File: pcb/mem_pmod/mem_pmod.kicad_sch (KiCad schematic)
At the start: 12 parts, among them J1 Conn_01x04_Pin, U1 74HC125D

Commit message: more or less completed schematic. Still needs caps/resistors or whatever
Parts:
- removed U1: 74HC125D, SOIC14_TOS, symbol 74HC125D:74HC125D
- removed VRAM1: APS6404L-3SQR-SN, APS6404L-3SQR-SN_APY, symbol ul_APS6404L-3SQR-SN:APS6404L-3SQR-SN
- added A0_NAND1, A0_NAND2, A1_NAND1: NC7SZ86FHX, MICROPAK2-6_1X1_ONS, symbol 74LVC1G57FW4-7:NC7SZ86FHX
- added J2: Conn_01x02_Pin, Connector_PinHeader_2.54mm:PinHeader_1x02_P2.54mm_Horizontal, symbol Connector:Conn_01x02_Pin
- added PMOD2: PMOD-Device-x2-Type-1A-GPIO, pmod-conn_6x2:pmod_pin_array_6x2, symbol pmod:PMOD-Device-x2-Type-1A-GPIO
- added U2: NL17SV32XV5T2G, SOT553-5_ONS, symbol NL17SV32XV5T2G:NL17SV32XV5T2G
- added XOR1: NC7SZ86FHX, MICROPAK2-6_1X1_ONS, symbol NC7SZ86FHX:NC7SZ86FHX
- J1: footprint (none) -> Connector_PinHeader_2.54mm:PinHeader_1x04_P2.54mm_Horizontal
- renumbered Clock_Divider to Clock_Divider1, Flash to Flash1, RAM0 to RAM1, RAM1 to RAM2, RAM2 to RAM3, VGA_DFLIP to VGA_DFLIP1, VGA_DFLIP to VGA_DFLIP2, VRAM0 to VRAM1
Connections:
- net RAM_VS0 is gone; now on net CS_V0: VRAM1.1 (/CE)
- net CS_A0: now also A0_NAND1.1 (A), A0_NAND2.1 (A), U2.1 (B), XOR1.1 (A)
- net CS_A1: now also A0_NAND2.2 (B), A1_NAND1.1 (A), U2.2 (A), XOR1.2 (B)
- net GND: now also A0_NAND1.3 (GND), A0_NAND2.3 (GND), A1_NAND1.3 (GND), PMOD2.11 (GND), PMOD2.5 (GND), U2.3 (GND), XOR1.3 (GND)
- net PMOD_B0: now also VGA_DFLIP1.3 (1D), VGA_DFLIP2.3 (1D)
- net PMOD_B1: now also VGA_DFLIP1.4 (2D), VGA_DFLIP2.4 (2D)
- net PMOD_B2: now also VGA_DFLIP1.7 (3D), VGA_DFLIP2.7 (3D)
- net RAM_CS0: now also A0_NAND1.4 (Y)
- net RAM_CS1: now also A1_NAND1.4 (Y)
- net RAM_CS2: now also U2.4 (Y)
- net RAM_CS3: now also A0_NAND2.4 (Y)
- net VCC: now also A0_NAND1.6 (VCC), A0_NAND2.6 (VCC), A1_NAND1.6 (VCC), PMOD2.12 (VCC), PMOD2.6 (VCC), U2.6 (VCC), XOR1.6 (VCC)
- net FLIP_2: now reaches VGA_DFLIP1.14 (6D)
- net FLIP_2: now also VGA_DFLIP1.6 (3Q)
- net VGA_B_1: now reaches VGA_DFLIP1.15 (6Q)
- net VGA_B_1: now also PMOD2.3 (IOA2)
- net VGA_G_1: now reaches VGA_DFLIP1.16 (7Q)
- net VGA_G_1: now also PMOD2.2 (IOA1)
- net FLIP_1: now reaches VGA_DFLIP1.17 (7D)
- net FLIP_1: now also VGA_DFLIP1.5 (2Q)
- net FLIP_0: now reaches VGA_DFLIP1.18 (8D)
- net FLIP_0: now also VGA_DFLIP1.2 (1Q)
- net VGA_R_1: now reaches VGA_DFLIP1.19 (8Q)
- net VGA_R_1: now also PMOD2.1 (IOA0)
- net VGA_R_0: now reaches VGA_DFLIP2.2 (1Q)
- net VGA_R_0: now also PMOD2.7 (IOB0)
- net VGA_G_0: now reaches VGA_DFLIP2.5 (2Q)
- net VGA_G_0: now also PMOD2.8 (IOB1)
- net VGA_B_0: now reaches VGA_DFLIP2.6 (3Q)
- net VGA_B_0: now also PMOD2.9 (IOB2)
- new net HSYNC: J2.2 (Pin_2), PMOD2.10 (IOB3)
- new net VSYNC: J2.1 (Pin_1), PMOD2.4 (IOA3)
- new net XOR_Result: A0_NAND1.2 (B), A1_NAND1.2 (B), XOR1.4 (Y)
- no-connect marks 0 -> 17
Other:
- moved on the sheet: VGA_DFLIP1, VGA_DFLIP2

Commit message: Add tinyvga and remove autosaves
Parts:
- removed PMOD2: PMOD-Device-x2-Type-1A-GPIO, pmod-conn_6x2:pmod_pin_array_6x2, symbol pmod:PMOD-Device-x2-Type-1A-GPIO
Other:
- added sheet vga (vga_submodule.kicad_sch)

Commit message: Abstracted CS stuff away into another sheet
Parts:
- removed A0_NAND1, A0_NAND2, A1_NAND1: NC7SZ86FHX, MICROPAK2-6_1X1_ONS, symbol 74LVC1G57FW4-7:NC7SZ86FHX
- removed U2: NL17SV32XV5T2G, SOT553-5_ONS, symbol NL17SV32XV5T2G:NL17SV32XV5T2G
- removed XOR1: NC7SZ86FHX, MICROPAK2-6_1X1_ONS, symbol NC7SZ86FHX:NC7SZ86FHX
- added C1: 10nF, Capacitor_SMD:C_01005_0402Metric, symbol Device:C
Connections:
- net FLIP_0: now also VGA_DFLIP2.18 (8D); no longer VGA_DFLIP1.18 (8D)
- net FLIP_1: now also VGA_DFLIP2.17 (7D); no longer VGA_DFLIP1.17 (7D)
- net FLIP_2: now also VGA_DFLIP2.14 (6D); no longer VGA_DFLIP1.14 (6D)
- net PRJ_Clock: now also Clock_Divider1.3 (*CLK); no longer Clock_Divider1.2 (CLK)
- net VCC: now also C1.1
- net VGA_B_1: now also VGA_DFLIP2.15 (6Q); no longer VGA_DFLIP1.15 (6Q)
- net VGA_G_1: now also VGA_DFLIP2.16 (7Q); no longer VGA_DFLIP1.16 (7Q)
- net VGA_R_1: now also VGA_DFLIP2.19 (8Q); no longer VGA_DFLIP1.19 (8Q)
- net VBB_CLK: now reaches Clock_Divider1.4 (VBB)
- net VBB_CLK: now also Clock_Divider1.2 (CLK)
- no-connect marks 17 -> 13
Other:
- added sheet CS_Circuit (cs_circuit.kicad_sch)

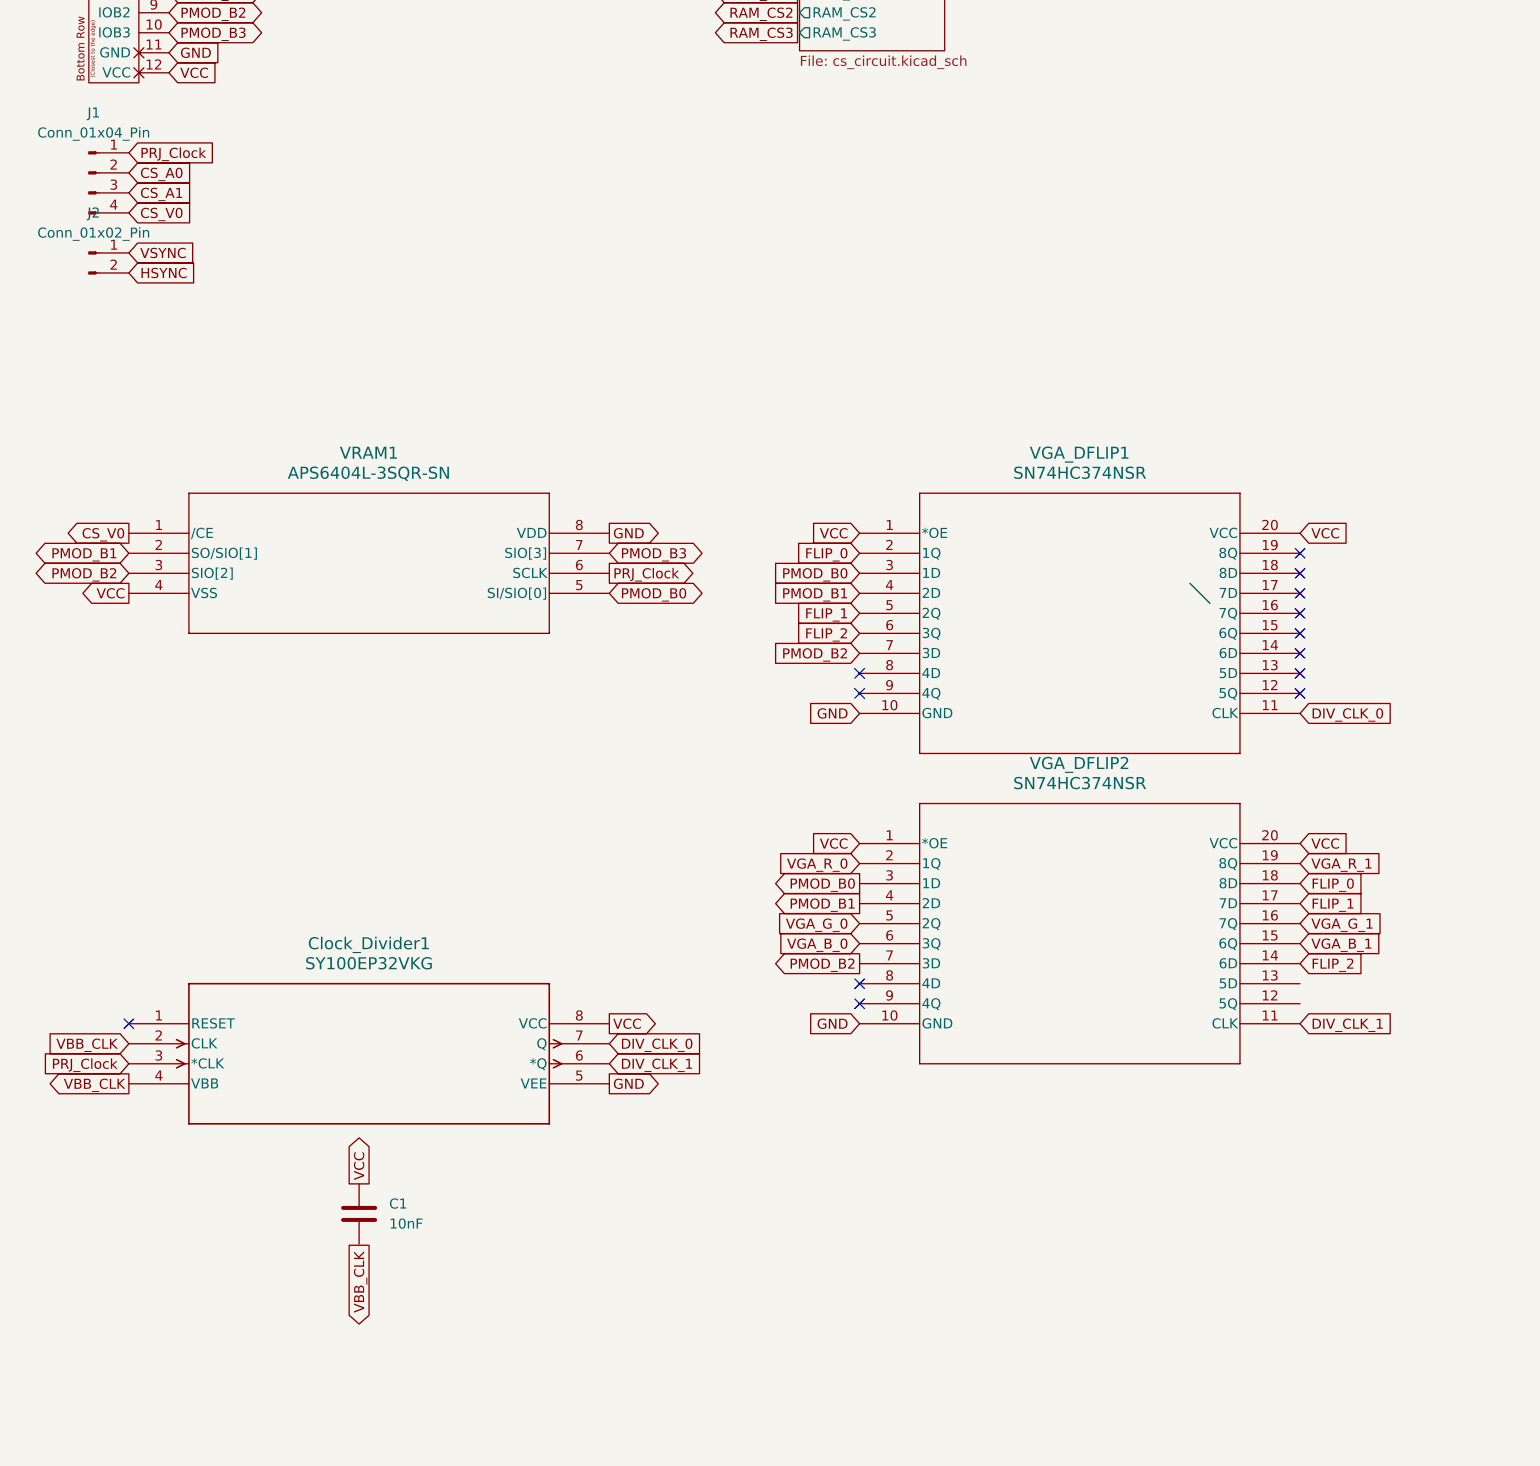
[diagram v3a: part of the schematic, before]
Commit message: change vram wiring
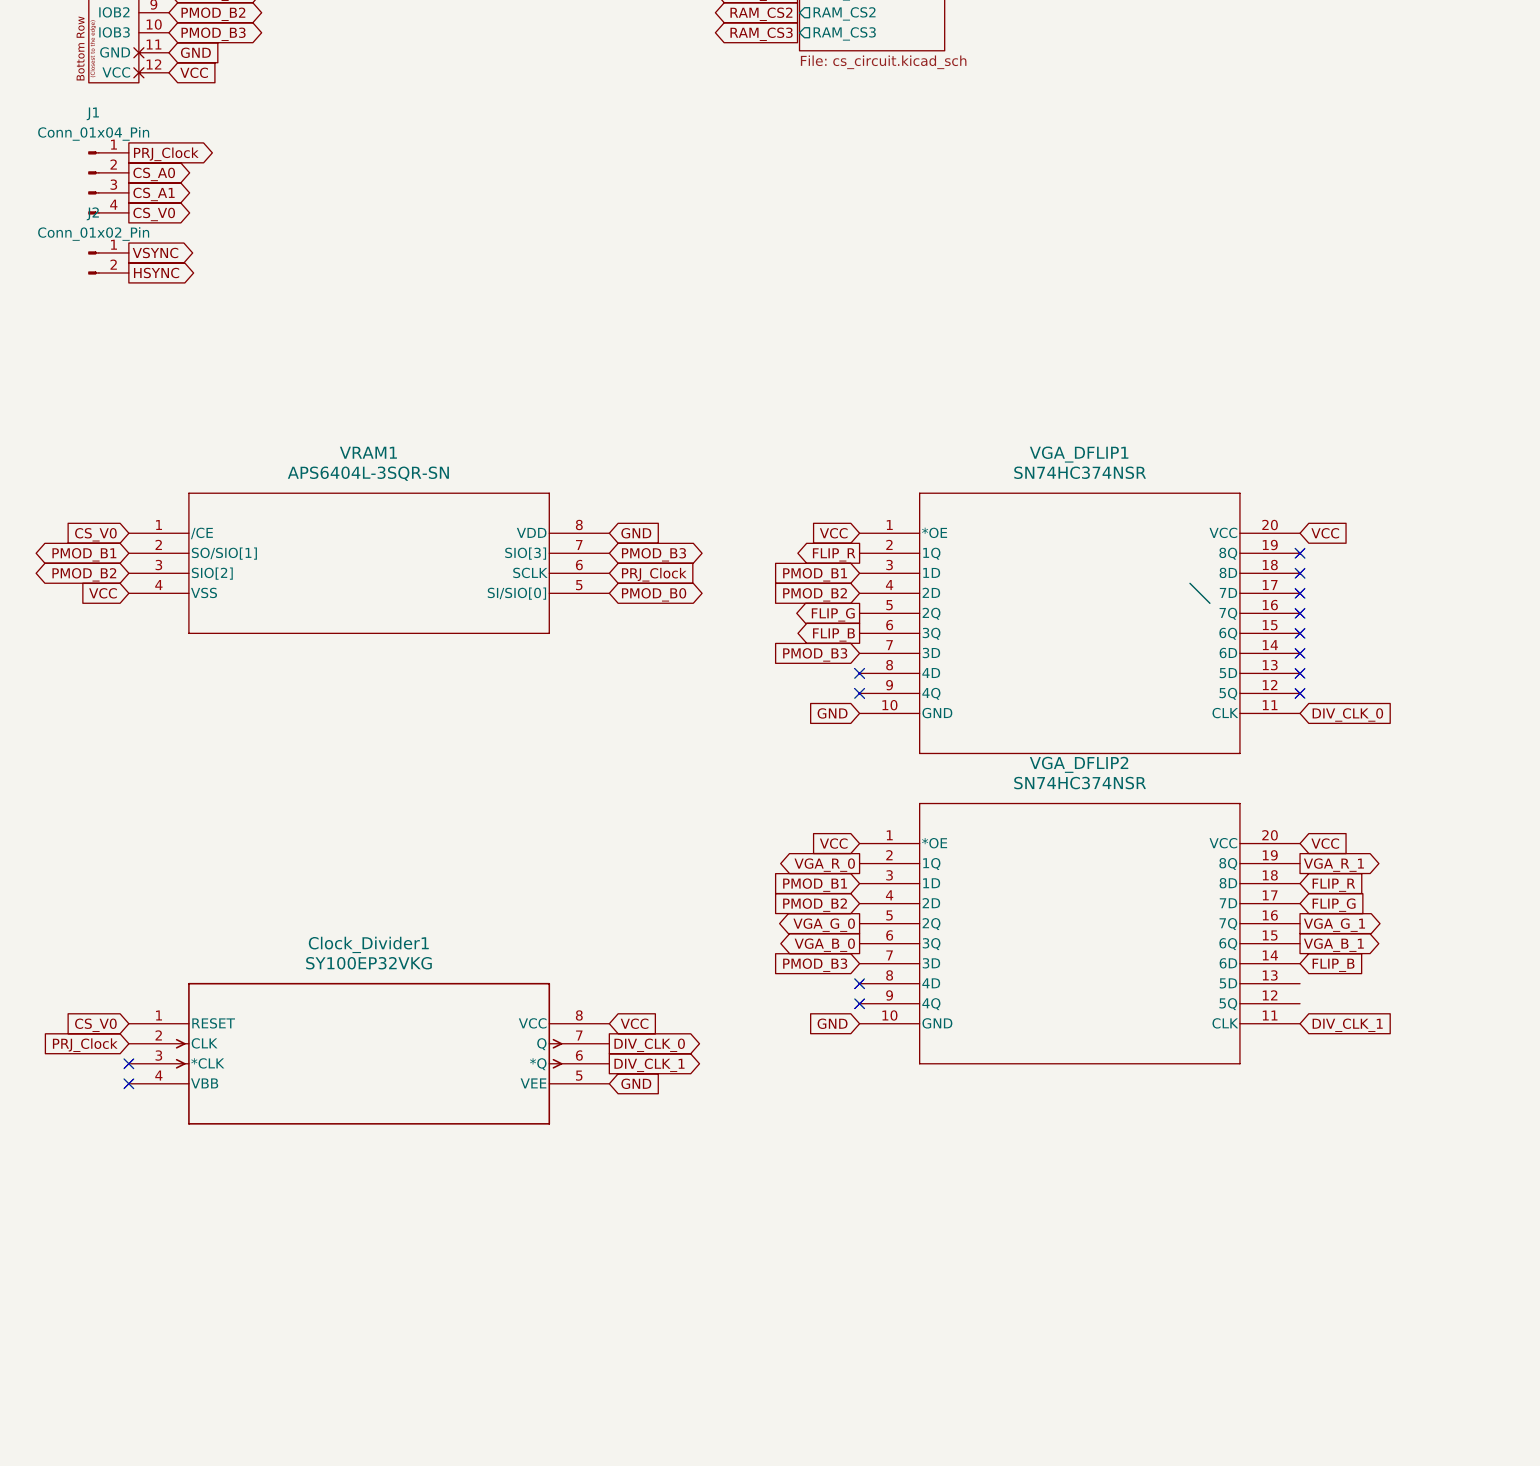
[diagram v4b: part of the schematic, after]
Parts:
- removed C1: 10nF, Capacitor_SMD:C_01005_0402Metric, symbol Device:C
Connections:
- net CS_V0: now also Clock_Divider1.1 (RESET)
- net PMOD_B0: no longer VGA_DFLIP1.3 (1D), VGA_DFLIP2.3 (1D)
- net PMOD_B1: now also VGA_DFLIP1.3 (1D), VGA_DFLIP2.3 (1D); no longer VGA_DFLIP1.4 (2D), VGA_DFLIP2.4 (2D)
- net PMOD_B2: now also VGA_DFLIP1.4 (2D), VGA_DFLIP2.4 (2D); no longer VGA_DFLIP1.7 (3D), VGA_DFLIP2.7 (3D)
- net PMOD_B3: now also VGA_DFLIP1.7 (3D), VGA_DFLIP2.7 (3D)
- net PRJ_Clock: now also Clock_Divider1.2 (CLK); no longer Clock_Divider1.3 (*CLK)
- net FLIP_0 renamed FLIP_R
- net FLIP_1 renamed FLIP_G
- net FLIP_2 renamed FLIP_B
- net VBB_CLK: no longer names the net of Clock_Divider1.4 (VBB)
- net VBB_CLK: no longer Clock_Divider1.2 (CLK)
- no-connect marks 13 -> 14
